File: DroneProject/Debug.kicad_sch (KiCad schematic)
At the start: 18 parts

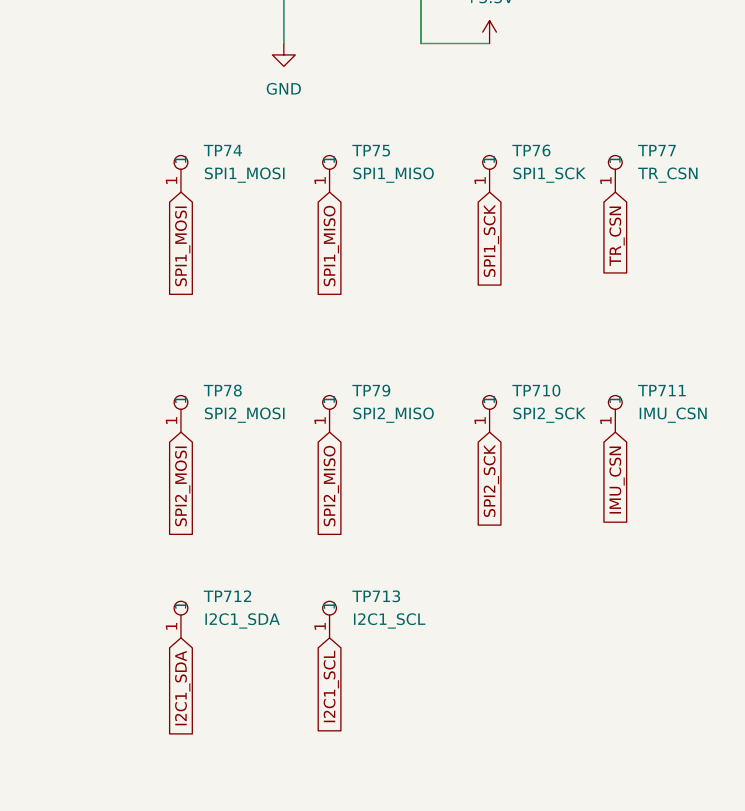
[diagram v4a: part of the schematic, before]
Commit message: Changed motor controller to higher pin count MCU.  Defined all the pins for 3x PWM control over 4 motors.  Renamed a couple of global IO signals to indicate MCU origin (C0 vs C1)
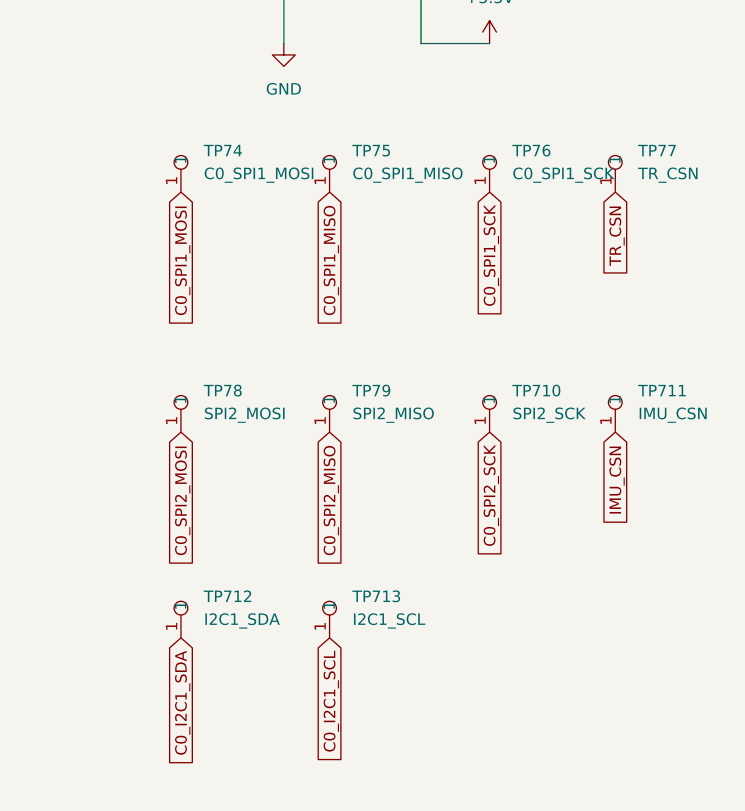
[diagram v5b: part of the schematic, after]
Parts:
- TP74: value SPI1_MOSI -> C0_SPI1_MOSI
- TP75: value SPI1_MISO -> C0_SPI1_MISO
- TP76: value SPI1_SCK -> C0_SPI1_SCK
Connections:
- net I2C1_SCL renamed C0_I2C1_SCL
- net I2C1_SDA renamed C0_I2C1_SDA
- net SPI1_MISO renamed C0_SPI1_MISO
- net SPI1_MOSI renamed C0_SPI1_MOSI
- net SPI1_SCK renamed C0_SPI1_SCK
- net SPI2_MISO renamed C0_SPI2_MISO
- net SPI2_MOSI renamed C0_SPI2_MOSI
- net SPI2_SCK renamed C0_SPI2_SCK
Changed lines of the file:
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@@
 		)
 	)
-	(global_label "SPI1_MISO"
+	(global_label "C0_SPI1_MISO"
 		(shape input)
 		(at 147.32 57.15 270)
@@
 		)
 		(property "Intersheetrefs" "${INTERSHEET_REFS}"
-			(at 147.32 69.9928 90)
+			(at 147.32 73.4399 90)
 			(effects
 				(font
@@
 		)
 	)
-	(global_label "I2C1_SCL"
+	(global_label "C0_I2C1_SCL"
 		(shape input)
 		(at 147.32 106.68 270)
@@
 		)
 		(property "Intersheetrefs" "${INTERSHEET_REFS}"
-			(at 147.32 118.0713 90)
+			(at 147.32 121.8813 90)
 			(effects
 				(font
@@
 		)
 	)
-	(global_label "SPI2_SCK"
+	(global_label "C0_SPI2_SCK"
 		(shape input)
 		(at 165.1 83.82 270)
@@
 		)
 		(property "Intersheetrefs" "${INTERSHEET_REFS}"
-			(at 165.1 95.8161 90)
+			(at 165.1 99.2632 90)
 			(effects
 				(font
@@
 		)
 	)
-	(global_label "SPI1_SCK"
+	(global_label "C0_SPI1_SCK"
 		(shape input)
 		(at 165.1 57.15 270)
@@
 		)
 		(property "Intersheetrefs" "${INTERSHEET_REFS}"
-			(at 165.1 69.1461 90)
+			(at 165.1 72.5932 90)
 			(effects
 				(font
@@
 		)
 	)
-	(global_label "I2C1_SDA"
+	(global_label "C0_I2C1_SDA"
 		(shape input)
 		(at 130.81 106.68 270)
@@
 		)
 		(property "Intersheetrefs" "${INTERSHEET_REFS}"
-			(at 130.81 118.4947 90)
+			(at 130.81 121.9418 90)
 			(effects
 				(font
@@
 		)
 	)
-	(global_label "SPI2_MOSI"
+	(global_label "C0_SPI2_MOSI"
 		(shape input)
 		(at 130.81 83.82 270)
@@
 		)
 		(property "Intersheetrefs" "${INTERSHEET_REFS}"
-			(at 130.81 96.6628 90)
+			(at 130.81 100.1099 90)
 			(effects
 				(font
@@
 		)
 	)
-	(global_label "SPI1_MOSI"
+	(global_label "C0_SPI1_MOSI"
 		(shape input)
 		(at 130.81 57.15 270)
@@
 		)
 		(property "Intersheetrefs" "${INTERSHEET_REFS}"
-			(at 130.81 69.9928 90)
+			(at 130.81 73.4399 90)
 			(effects
 				(font
@@
 		)
 	)
-	(global_label "SPI2_MISO"
+	(global_label "C0_SPI2_MISO"
 		(shape input)
 		(at 147.32 83.82 270)
@@
 		)
 		(property "Intersheetrefs" "${INTERSHEET_REFS}"
-			(at 147.32 96.6628 90)
+			(at 147.32 100.1099 90)
 			(effects
 				(font
@@
 			)
 		)
-		(property "Value" "SPI1_MOSI"
+		(property "Value" "C0_SPI1_MOSI"
 			(at 133.35 55.1179 0)
 			(effects
@@
 			)
 		)
-		(property "Value" "SPI1_SCK"
+		(property "Value" "C0_SPI1_SCK"
 			(at 167.64 55.1179 0)
 			(effects
@@
 			)
 		)
-		(property "Value" "SPI1_MISO"
+		(property "Value" "C0_SPI1_MISO"
 			(at 149.86 55.1179 0)
 			(effects
